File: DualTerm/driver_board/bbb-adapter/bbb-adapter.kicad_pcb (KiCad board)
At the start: 2 copper layers, 15 parts, among them J1 CONN_01X03, J2 Screw_Terminal_1x03, J3 GS3, P2 CONN_01X06, P3 CONN_01X06, P8 CONN_02X23, P9 CONN_02X23, Q1 Q_NMOS_GSD, U1 74LS244, U2 74LS32

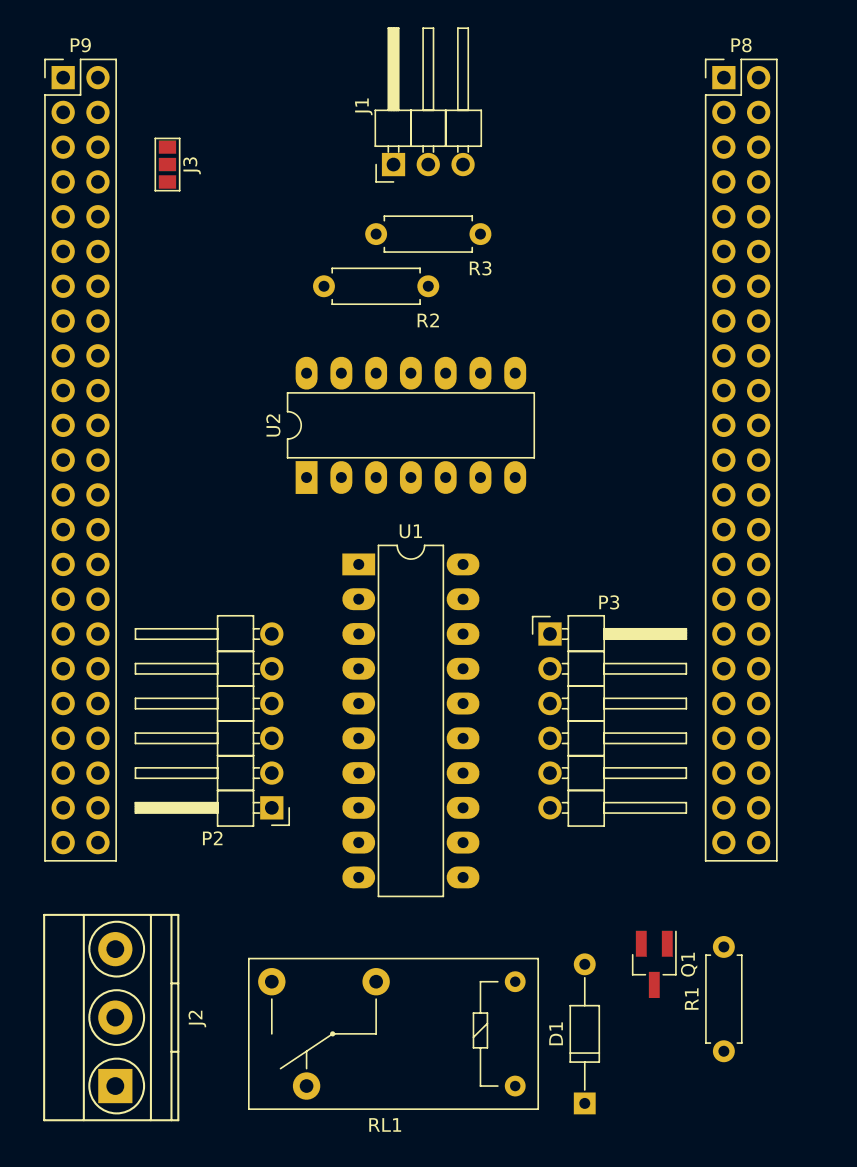
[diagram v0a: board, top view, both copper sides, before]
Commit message: board ordered
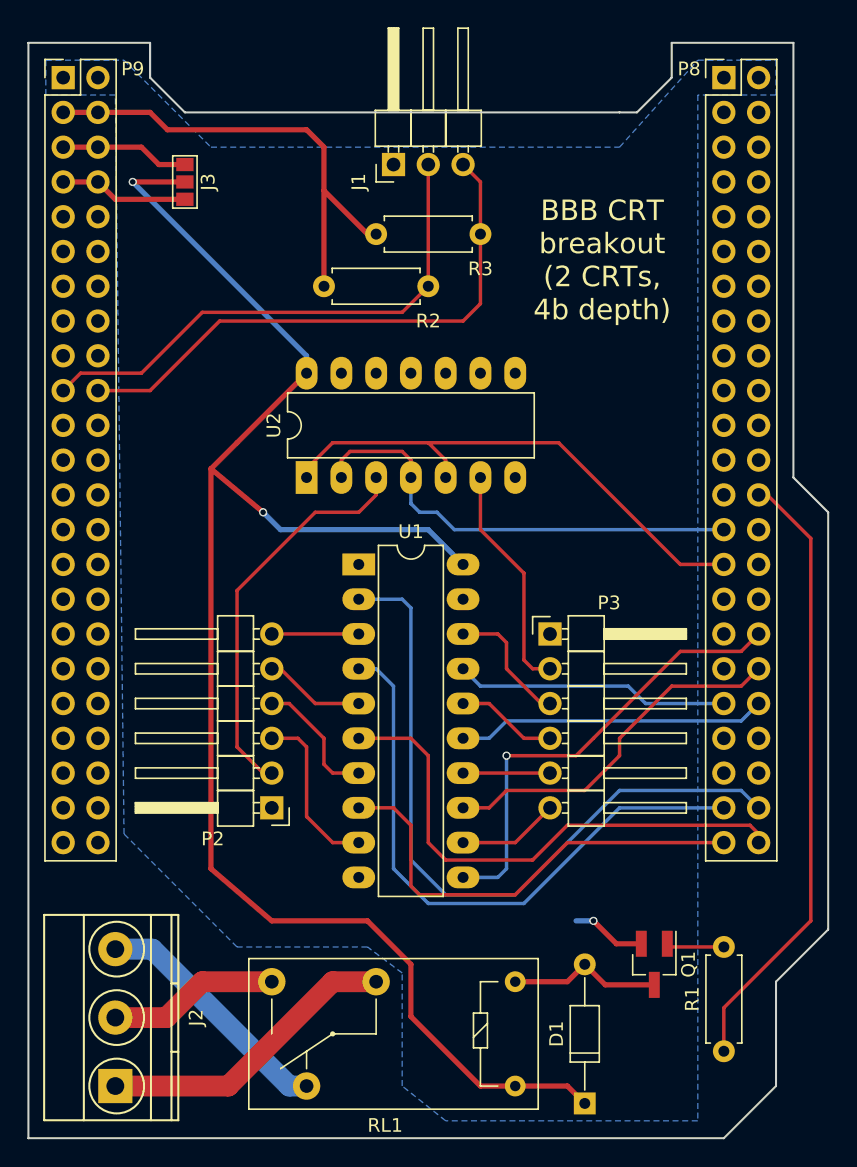
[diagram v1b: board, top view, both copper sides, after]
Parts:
- moved J3 1.80 mm to (57.1, 77.5)
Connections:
- U2 pad 3: CSYNC_A -> CSYNC_B
- U2 pad 4: BB_HSYNC -> BB_VSYNC
- U2 pad 5: BB_VSYNC -> BB_HSYNC
- U2 pad 6: CSYNC_B -> CSYNC_A
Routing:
- net VCC: track 0.00 -> 119.7 mm, vias 0 -> 3
- net BB_LCD3: track 0.00 -> 52.6 mm
- net BB_GPIO1_29: track 0.00 -> 45.2 mm
- net BB_LCD2: track 0.00 -> 44.5 mm
- net BB_I2C2_SDA: track 0.00 -> 41.3 mm
- net BB_I2C2_SCL: track 0.00 -> 38.7 mm
- net BB_HSYNC: track 0.00 -> 38.7 mm
- net BB_LCD1: track 0.00 -> 38.6 mm
- net +3V3: track 0.00 -> 35.4 mm
- net BB_LCD11: track 0.00 -> 33.8 mm, vias 0 -> 1
- net BB_VSYNC: track 0.00 -> 33.7 mm
- net BB_LCD0: track 0.00 -> 33.5 mm
- net CSYNC_B: track 0.00 -> 29.1 mm
- net BB_LCD10: track 0.00 -> 26.5 mm
- net BB_LCD9: track 0.00 -> 22.6 mm
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- added copper zone on B.Cu, net GND
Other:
- board outline added: 58.4 x 80 mm
- board text added: "BBB CRT breakout (2 CRTs, 4b depth)"
